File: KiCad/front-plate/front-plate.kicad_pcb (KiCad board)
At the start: 2 copper layers, 325.1 x 124.5 mm, 87 parts, among them SW1 keys, SW10 keys, SW11 keys, SW12 keys, SW13 keys, SW14 keys, SW15 keys, SW16 keys, SW17 keys, SW18 keys, SW19 keys, SW2 keys, SW20 keys, SW21 keys, SW22 keys, SW23 keys, SW24 keys, SW25 keys, SW26 keys, SW27 keys, SW28 keys, SW29 keys, SW3 keys, SW30 keys, SW31 keys, SW32 keys, SW33 keys, SW34 keys, SW35 keys, SW36 keys, SW37 keys, SW38 keys, SW39 keys, SW4 keys, SW40 keys, SW41 keys, SW42 keys, SW43 keys, SW44 keys, SW45 keys, SW46 keys, SW47 keys, SW48 keys, SW49 keys, SW5 keys, SW50 keys, SW51 keys, SW52 keys, SW53 keys, SW54 keys, SW55 keys, SW56 keys, SW57 keys, SW58 keys, SW59 keys, SW6 keys, SW60 keys, SW61 keys, SW62 keys, SW63 keys, SW64 keys, SW65 keys, SW66 keys, SW67 keys, SW68 keys, SW69 keys, SW7 keys, SW70 keys, SW71 keys, SW72 keys, SW73 keys, SW75 keys, SW8 keys, SW9 keys

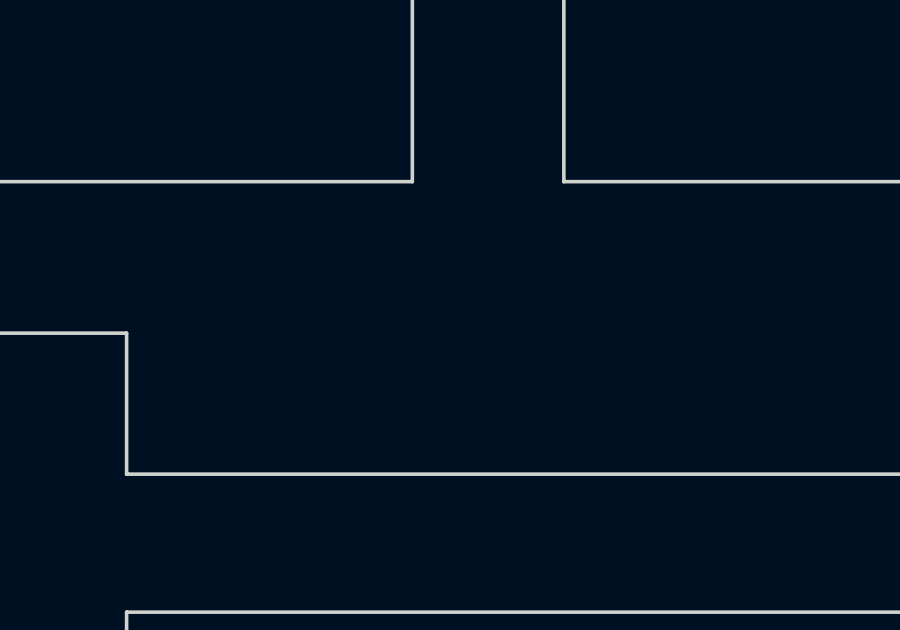
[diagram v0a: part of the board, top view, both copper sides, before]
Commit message: Corrected fab plots (and jlc marker) - feedback from jlc support
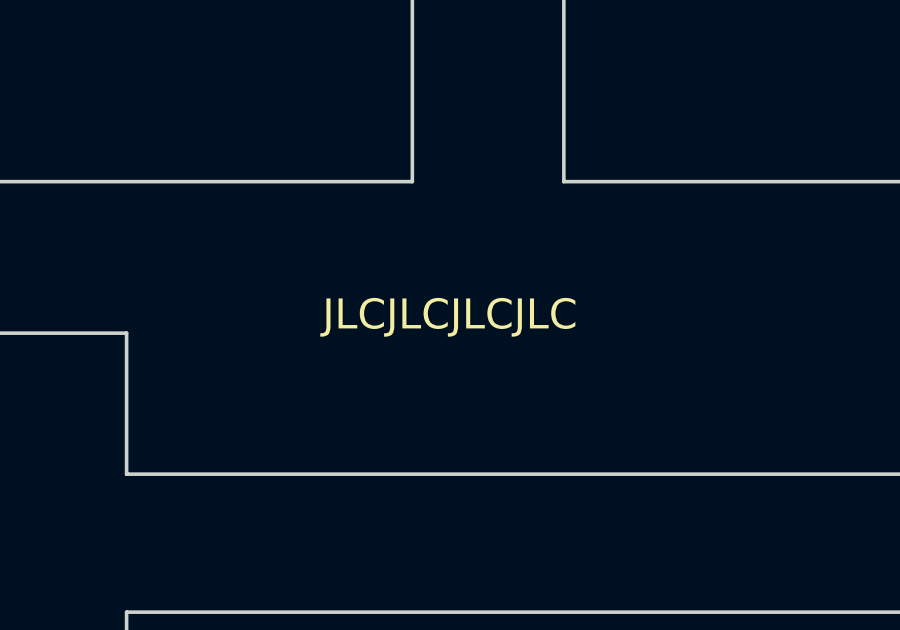
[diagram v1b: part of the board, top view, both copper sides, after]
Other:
- board text added: "JLCJLCJLCJLC"
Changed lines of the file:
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@@
       (drillshape 0)
       (scaleselection 1)
-      (outputdirectory "jlcpcb-20230704")
+      (outputdirectory "jlcpcb-20230705")
     )
   )
@@
   (gr_arc (start 61.2775 232.41) (mid 59.481449 231.666051) (end 58.7375 229.87) (layer "Edge.Cuts") (width 0.1))
   (gr_line (start 383.8575 189.23) (end 383.8575 110.49) (layer "Edge.Cuts") (width 0.1))
+  (gr_text "JLCJLCJLCJLC" (at 222.5675 208.28) (layer "F.SilkS")
+    (effects (font (size 1 1) (thickness 0.15)))
+  )
   (gr_text "6.25u, 7u, 8u PCB mount stabilizers not 6.5u\nFor 6.25, 6.5u, 7u, 8u spacebar use cutouts" (at 271.4625 263.525) (layer "Cmts.User")
     (effects (font (size 1 1) (thickness 0.15)))

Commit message: enlarge holes and match up to main pcb
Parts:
- H10, H11, H12, H13, H14, H15, H16, H7, H8, H9: footprint MountingHole:MountingHole_2.7mm_M2.5_DIN965_Pad -> MountingHole:MountingHole_3.2mm_M3_DIN965_Pad

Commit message: larger LED holes, remove silkscreen designators
update LED holes in schematic

larger LED holes, remove silkscreens
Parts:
- LD1, LD2, LD3: footprint MountingHole:MountingHole_4.3mm_M4 -> MountingHole:MountingHole_5.5mm
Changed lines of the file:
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@@
     (property "Sheetname" "")
     (attr exclude_from_pos_files)
-    (fp_text reference "H13" (at 0 -3.8) (layer "F.SilkS")
+    (fp_text reference "H13" (at 0 -3.8) (layer "F.SilkS") hide
       (effects (font (size 1 1) (thickness 0.15)))
     )
@@
     (property "Sheetname" "")
     (attr exclude_from_pos_files)
-    (fp_text reference "H11" (at 0 -3.8) (layer "F.SilkS")
+    (fp_text reference "H11" (at 0 -3.8) (layer "F.SilkS") hide
       (effects (font (size 1 1) (thickness 0.15)))
     )
@@
     (property "Sheetname" "")
     (attr exclude_from_pos_files)
-    (fp_text reference "H16" (at 0 -3.8) (layer "F.SilkS")
+    (fp_text reference "H16" (at 0 -3.8) (layer "B.SilkS") hide
       (effects (font (size 1 1) (thickness 0.15)))
     )
@@
     (property "Sheetname" "")
     (attr exclude_from_pos_files)
-    (fp_text reference "H14" (at 0 -3.8) (layer "F.SilkS")
+    (fp_text reference "H14" (at 0 -3.8) (layer "B.SilkS") hide
       (effects (font (size 1 1) (thickness 0.15)))
     )
@@
     (property "Sheetname" "")
     (attr exclude_from_pos_files)
-    (fp_text reference "H12" (at 0 -3.8) (layer "F.SilkS")
+    (fp_text reference "H12" (at 0 -3.8) (layer "F.SilkS") hide
       (effects (font (size 1 1) (thickness 0.15)))
     )
@@
     (property "Sheetname" "")
     (attr exclude_from_pos_files)
-    (fp_text reference "H15" (at 0 -3.8) (layer "F.SilkS")
+    (fp_text reference "H15" (at 0 -3.8) (layer "F.SilkS") hide
       (effects (font (size 1 1) (thickness 0.15)))
     )
@@
     (fp_line (start 7.1 7.1) (end -7.1 7.1) (layer "F.Fab") (width 0.1))
   )
-  (footprint "MountingHole:MountingHole_4.3mm_M4" (layer "F.Cu")
+  (footprint "MountingHole:MountingHole_5.5mm" (layer "F.Cu")
     (at 73.9775 224.79 -90)
-    (descr "Mounting Hole 4.3mm, no annular, M4")
-    (tags "mounting hole 4.3mm no annular m4")
+    (descr "Mounting Hole 5.5mm, no annular")
+    (tags "mounting hole 5.5mm no annular")
     (property "Sheetfile" "front-plate.kicad_sch")
     (property "Sheetname" "")
     (attr exclude_from_pos_files)
-    (fp_text reference "LD3" (at 0 -5.3 -90) (layer "F.SilkS") hide
-      (effects (font (size 1 1) (thickness 0.15)))
-    )
-    (fp_text value "MountingHole" (at 0 5.3 -90) (layer "F.Fab")
+    (fp_text reference "LD3" (at 0 -6.5 -90) (layer "B.SilkS") hide
+      (effects (font (size 1 1) (thickness 0.15)))
+    )
+    (fp_text value "MountingHole" (at 0 6.5 -90) (layer "F.Fab")
       (effects (font (size 1 1) (thickness 0.15)))
     )
@@
       (effects (font (size 1 1) (thickness 0.15)))
     )
-    (fp_circle (center 0 0) (end 4.3 0) (layer "Cmts.User") (width 0.15) (fill none))
-    (fp_circle (center 0 0) (end 4.55 0) (layer "F.CrtYd") (width 0.05) (fill none))
-    (pad "" np_thru_hole circle (at 0 0 270) (size 4.3 4.3) (drill 4.3) (layers *.Cu *.Mask))
+    (fp_circle (center 0 0) (end 5.5 0) (layer "Cmts.User") (width 0.15) (fill none))
+    (fp_circle (center 0 0) (end 5.75 0) (layer "F.CrtYd") (width 0.05) (fill none))
+    (pad "" np_thru_hole circle (at 0 0 270) (size 5.5 5.5) (drill 5.5) (layers *.Cu *.Mask))
   )
   (footprint "Holes:Cherry_MX_panel_cutout" (layer "F.Cu")
@@
     (fp_line (start 7.1 -7.1) (end 7.1 7.1) (layer "F.Fab") (width 0.1))
   )
-  (footprint "MountingHole:MountingHole_4.3mm_M4" (layer "F.Cu")
+  (footprint "MountingHole:MountingHole_5.5mm" (layer "F.Cu")
     (at 94.2975 224.79 -90)
-    (descr "Mounting Hole 4.3mm, no annular, M4")
-    (tags "mounting hole 4.3mm no annular m4")
+    (descr "Mounting Hole 5.5mm, no annular")
+    (tags "mounting hole 5.5mm no annular")
     (property "Sheetfile" "front-plate.kicad_sch")
     (property "Sheetname" "")
     (attr exclude_from_pos_files)
-    (fp_text reference "LD2" (at 0 -5.3 -90) (layer "F.SilkS") hide
-      (effects (font (size 1 1) (thickness 0.15)))
-    )
-    (fp_text value "MountingHole" (at 0 5.3 -90) (layer "F.Fab")
+    (fp_text reference "LD2" (at 0 -6.5 -90) (layer "B.SilkS") hide
+      (effects (font (size 1 1) (thickness 0.15)))
+    )
+    (fp_text value "MountingHole" (at 0 6.5 -90) (layer "F.Fab")
       (effects (font (size 1 1) (thickness 0.15)))
     )
@@
       (effects (font (size 1 1) (thickness 0.15)))
     )
-    (fp_circle (center 0 0) (end 4.3 0) (layer "Cmts.User") (width 0.15) (fill none))
-    (fp_circle (center 0 0) (end 4.55 0) (layer "F.CrtYd") (width 0.05) (fill none))
-    (pad "" np_thru_hole circle (at 0 0 270) (size 4.3 4.3) (drill 4.3) (layers *.Cu *.Mask))
+    (fp_circle (center 0 0) (end 5.5 0) (layer "Cmts.User") (width 0.15) (fill none))
+    (fp_circle (center 0 0) (end 5.75 0) (layer "F.CrtYd") (width 0.05) (fill none))
+    (pad "" np_thru_hole circle (at 0 0 270) (size 5.5 5.5) (drill 5.5) (layers *.Cu *.Mask))
   )
   (footprint "Holes:Cherry_MX_panel_cutout" (layer "F.Cu")
@@
     (property "Sheetname" "")
     (attr exclude_from_pos_files)
-    (fp_text reference "H8" (at 0 -3.8) (layer "F.SilkS")
+    (fp_text reference "H8" (at 4.445 -1.905) (layer "B.SilkS") hide
       (effects (font (size 1 1) (thickness 0.15)))
     )
@@
     (fp_line (start 7.1 7.1) (end -7.1 7.1) (layer "F.Fab") (width 0.1))
   )
-  (footprint "MountingHole:MountingHole_4.3mm_M4" (layer "F.Cu")
+  (footprint "MountingHole:MountingHole_5.5mm" (layer "F.Cu")
     (at 114.6175 224.79 -90)
-    (descr "Mounting Hole 4.3mm, no annular, M4")
-    (tags "mounting hole 4.3mm no annular m4")
+    (descr "Mounting Hole 5.5mm, no annular")
+    (tags "mounting hole 5.5mm no annular")
     (property "Sheetfile" "front-plate.kicad_sch")
     (property "Sheetname" "")
     (attr exclude_from_pos_files)
-    (fp_text reference "LD1" (at 0 -5.3 -90) (layer "F.SilkS") hide
-      (effects (font (size 1 1) (thickness 0.15)))
-    )
-    (fp_text value "MountingHole" (at 0 5.3 -90) (layer "F.Fab")
+    (fp_text reference "LD1" (at 0 -6.5 -90) (layer "B.SilkS") hide
+      (effects (font (size 1 1) (thickness 0.15)))
+    )
+    (fp_text value "MountingHole" (at 0 6.5 -90) (layer "F.Fab")
       (effects (font (size 1 1) (thickness 0.15)))
     )
@@
       (effects (font (size 1 1) (thickness 0.15)))
     )
-    (fp_circle (center 0 0) (end 4.3 0) (layer "Cmts.User") (width 0.15) (fill none))
-    (fp_circle (center 0 0) (end 4.55 0) (layer "F.CrtYd") (width 0.05) (fill none))
-    (pad "" np_thru_hole circle (at 0 0 270) (size 4.3 4.3) (drill 4.3) (layers *.Cu *.Mask))
+    (fp_circle (center 0 0) (end 5.5 0) (layer "Cmts.User") (width 0.15) (fill none))
+    (fp_circle (center 0 0) (end 5.75 0) (layer "F.CrtYd") (width 0.05) (fill none))
+    (pad "" np_thru_hole circle (at 0 0 270) (size 5.5 5.5) (drill 5.5) (layers *.Cu *.Mask))
   )
   (footprint "Holes:Cherry_MX_panel_cutout" (layer "F.Cu")
@@
     (property "Sheetname" "")
     (attr exclude_from_pos_files)
-    (fp_text reference "H7" (at 0 -3.8) (layer "F.SilkS")
+    (fp_text reference "H7" (at 4.445 -1.905) (layer "B.SilkS") hide
       (effects (font (size 1 1) (thickness 0.15)))
     )
@@
     (property "Sheetname" "")
     (attr exclude_from_pos_files)
-    (fp_text reference "H10" (at 0 -3.8) (layer "F.SilkS")
+    (fp_text reference "H10" (at 0 -3.8) (layer "F.SilkS") hide
       (effects (font (size 1 1) (thickness 0.15)))
     )
@@
     (property "Sheetname" "")
     (attr exclude_from_pos_files)
-    (fp_text reference "H9" (at 0 -3.8) (layer "F.SilkS")
+    (fp_text reference "H9" (at 0 -3.8) (layer "F.SilkS") hide
       (effects (font (size 1 1) (thickness 0.15)))
     )
@@
   (gr_arc (start 61.2775 232.41) (mid 59.481449 231.666051) (end 58.7375 229.87) (layer "Edge.Cuts") (width 0.1))
   (gr_line (start 383.8575 189.23) (end 383.8575 110.49) (layer "Edge.Cuts") (width 0.1))
-  (gr_text "JLCJLCJLCJLC" (at 222.5675 208.28) (layer "F.SilkS")
+  (gr_text "JLCJLCJLCJLC" (at 221.9325 210.82) (layer "F.SilkS")
     (effects (font (size 1 1) (thickness 0.15)))
   )
